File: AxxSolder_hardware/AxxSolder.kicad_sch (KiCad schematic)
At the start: 148 parts, among them IC1 TLV76733DRVR, IC2 OPA2387DSGT, IC3 LMR54406DBVR, IC4 STM32G431CBT6, IC5 TPD4E1U06DBVR, IC6 STUSB4500QTR, IC7 MAX16171ATA_VY+T, IC8 LTC4440AHMS8E, IC9 INA281A5QDBVRQ1, J1 USB4110-GF-A, J2 691243110009, J3 TSW-102-07-T-S, J4 61300611821, J5 TSW-102-07-T-S, J6 TSW-102-07-T-S, Q1 STL9P3LLH6, Q2 STL10N3LLH5, Q3 2N7002NXAKR, U2 PEC11J-9215F-S0015, U3 BSC014N04LS

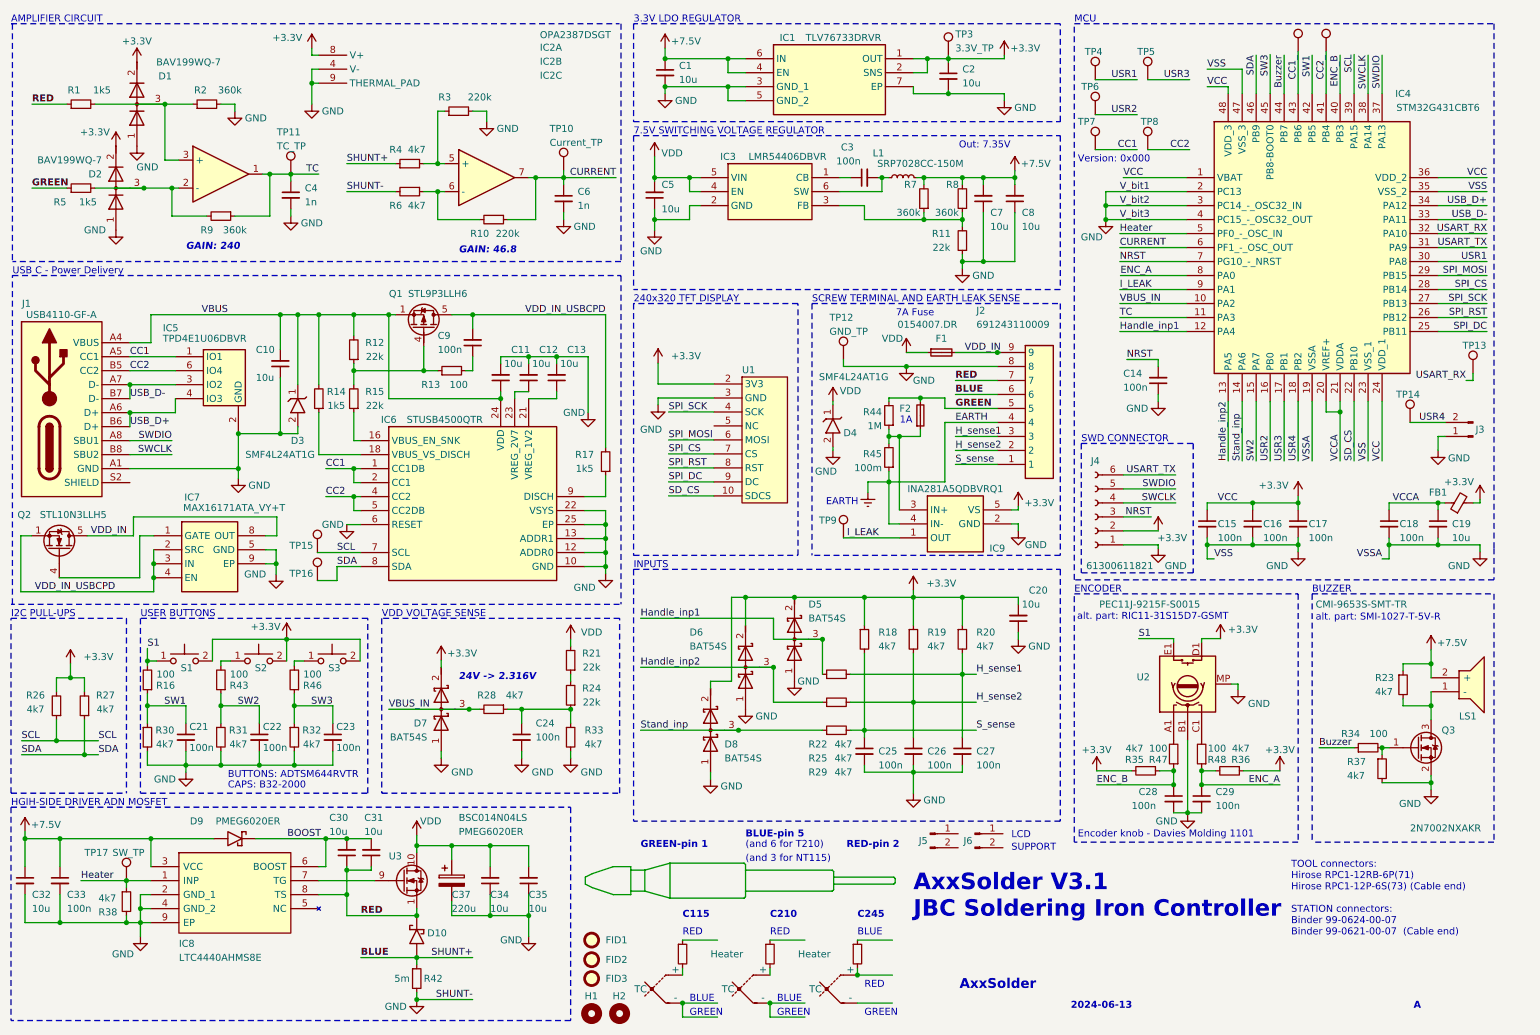
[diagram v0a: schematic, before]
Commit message: Updates on schematic and board layout to hw3_1, optimizations and improvement on layout
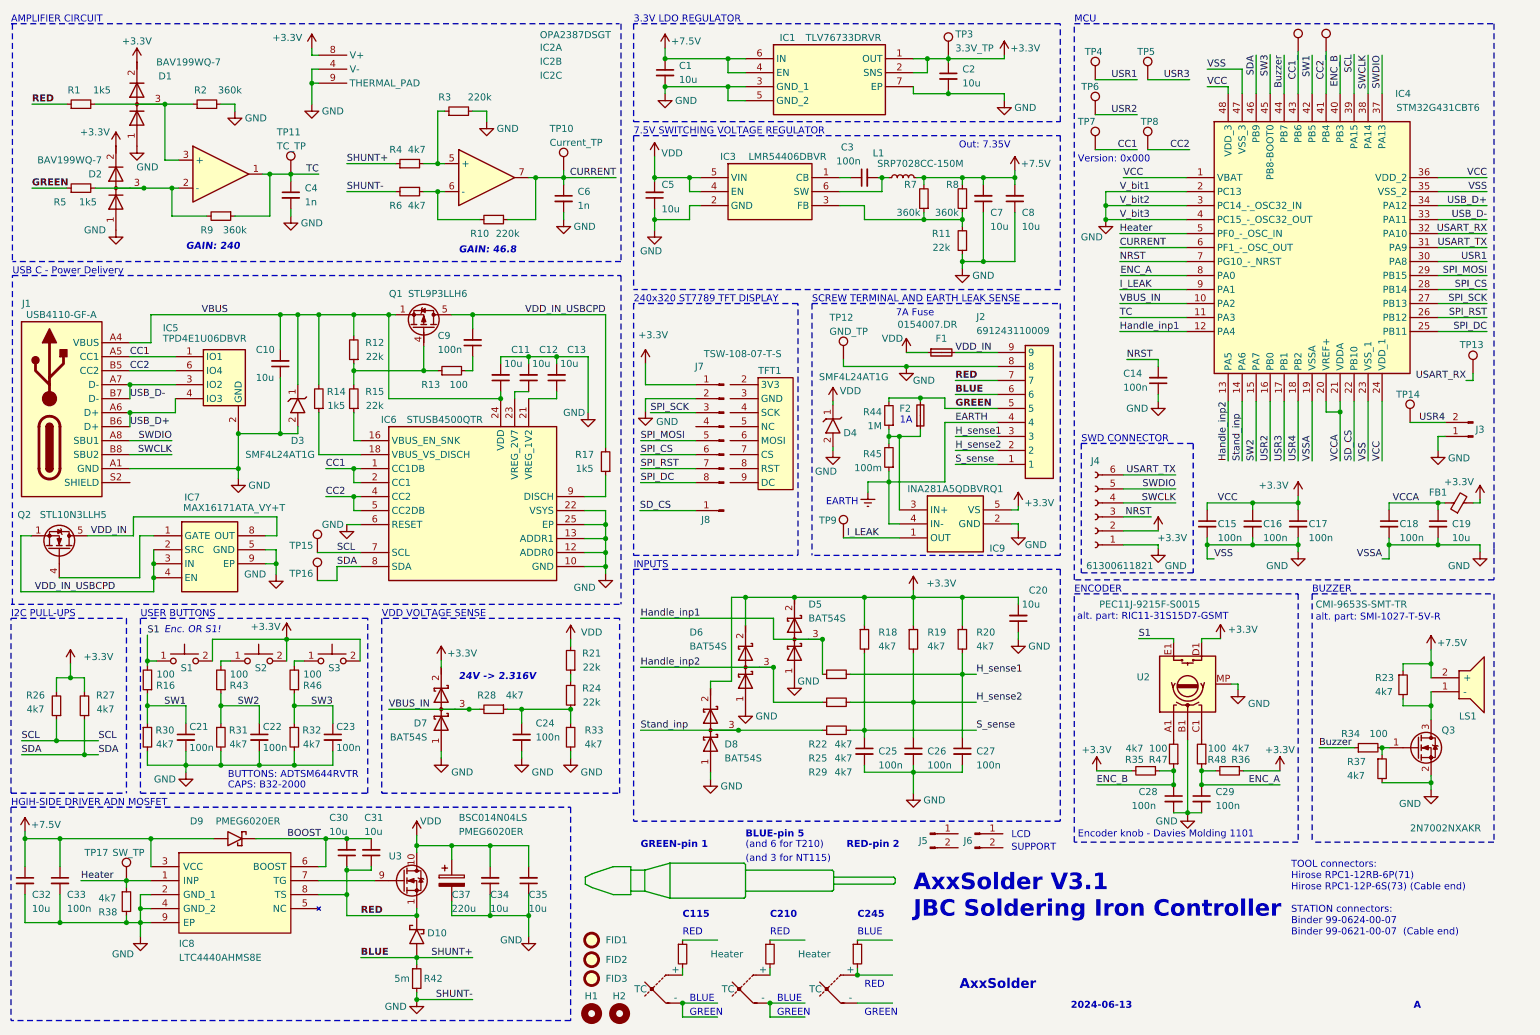
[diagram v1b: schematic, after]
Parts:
- added J7: TSW-108-07-T-S, TSW-108-XX-YY-S, symbol TSW-108-07-T-S:TSW-108-07-T-S
- added J8: Conn_01x01_Pin, symbol Connector:Conn_01x01_Pin
- D5, D6, D7, D8: Manufacturer_Name Diotec Semiconductor -> Nexperia; Manufacturer_Part_Number BAT54S -> BAT54S,215; Mouser Part Number 637-BAT54S -> 771-BAT54S-T/R; Mouser Price/Stock https://www.mouser.co.uk/ProductDetail/Diotec-Semiconductor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 -> https://www.mouser.co.uk/ProductDetail/Nexperia/BAT54S215?q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
- S1: now left out of the parts list
- TP13: footprint Connector_PinSocket_2.54mm:PinSocket_1x01_P2.54mm_Vertical -> footprints:TSW-101-XX-YY-S
- renumbered U1 to TFT1
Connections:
- net +3.3V: now also J7.1 (Pin_1); no longer TFT1.2 (3V3)
- net GND: now also J7.2 (Pin_2); no longer TFT1.3 (GND)
- net SD_CS: now also J8.1 (Pin_1); no longer TFT1.10 (SDCS)
- net SPI_CS: now also J7.6 (Pin_6); no longer TFT1.7 (CS)
- net SPI_DC: now also J7.8 (Pin_8); no longer TFT1.9 (DC)
- net SPI_MOSI: now also J7.5 (Pin_5); no longer TFT1.6 (MOSI)
- net SPI_RST: now also J7.7 (Pin_7); no longer TFT1.8 (RST)
- net SPI_SCK: now also J7.3 (Pin_3); no longer TFT1.4 (SCK)
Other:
- note added: "240x320 ST7789 TFT DISPLAY"
- note added: "Enc. OR S1!"
- note removed: "240x320 TFT DISPLAY"

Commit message: Update footprint name of STL9P3LLH6 to be correct
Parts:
- Q1: footprint footprints:STL20N6F7 -> footprints:STL9P3LLH6
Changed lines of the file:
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@@
       (effects (font (size 1.27 1.27)))
     )
-    (property "Footprint" "footprints:STL20N6F7" (at 69.85 162.992 0)
+    (property "Footprint" "footprints:STL9P3LLH6" (at 69.85 162.992 0)
       (effects (font (size 1.27 1.27)) (justify left top) hide)
     )

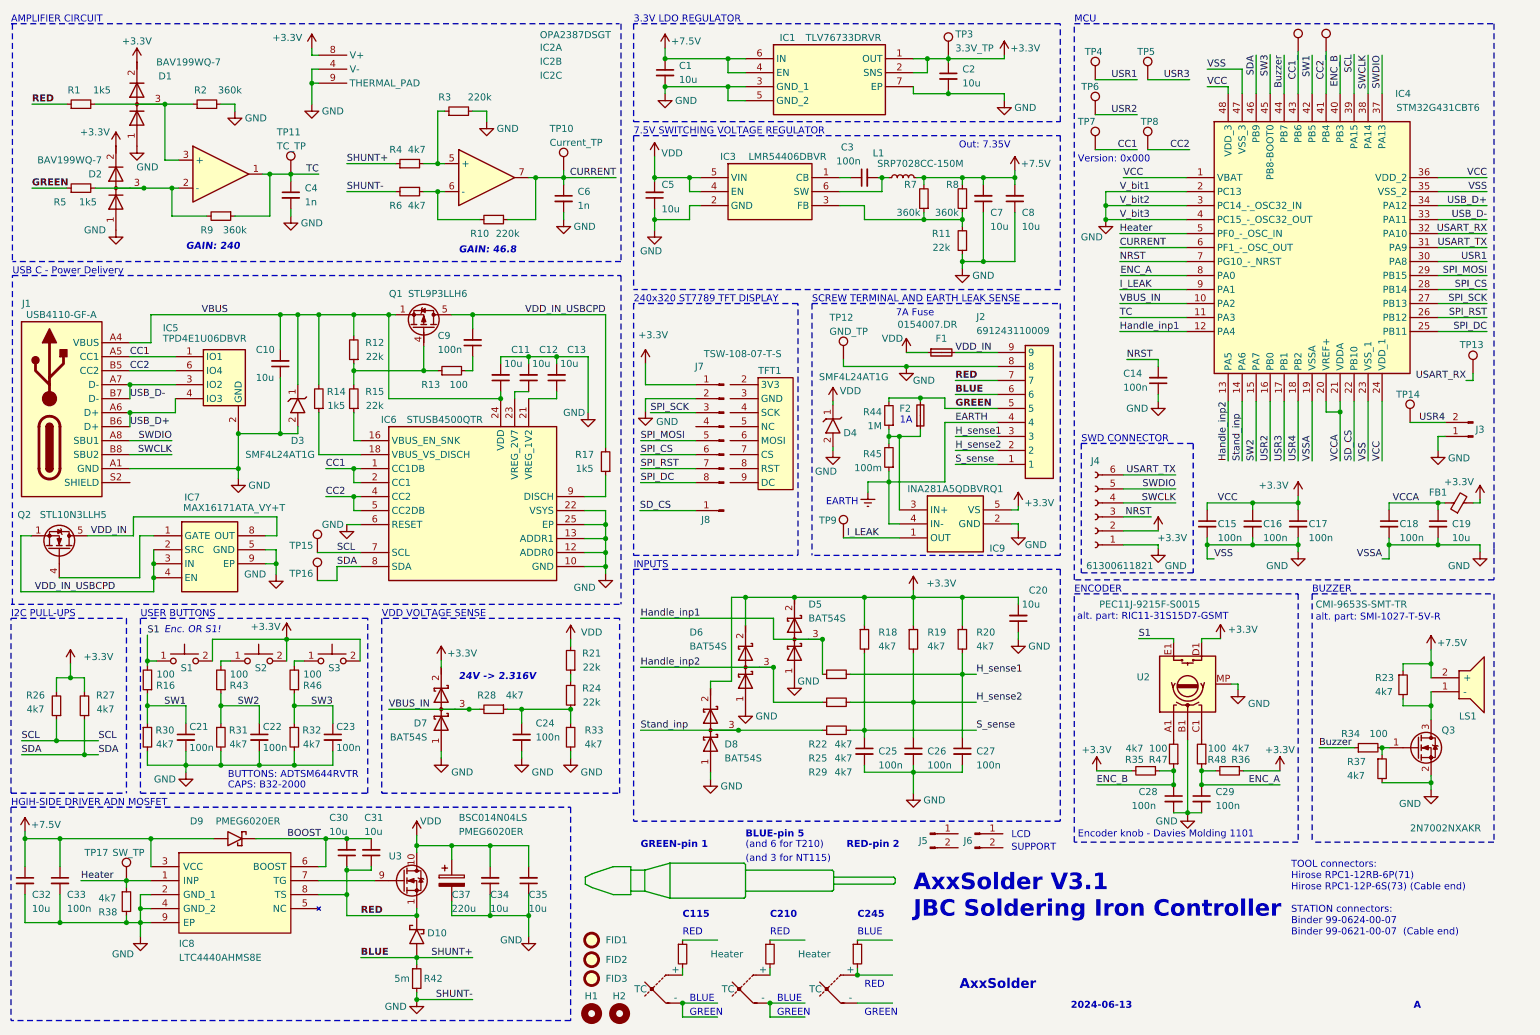
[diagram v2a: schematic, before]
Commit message: Update hardware to 3.2 with changes in layout and addition of series resistors on op-amp outputs
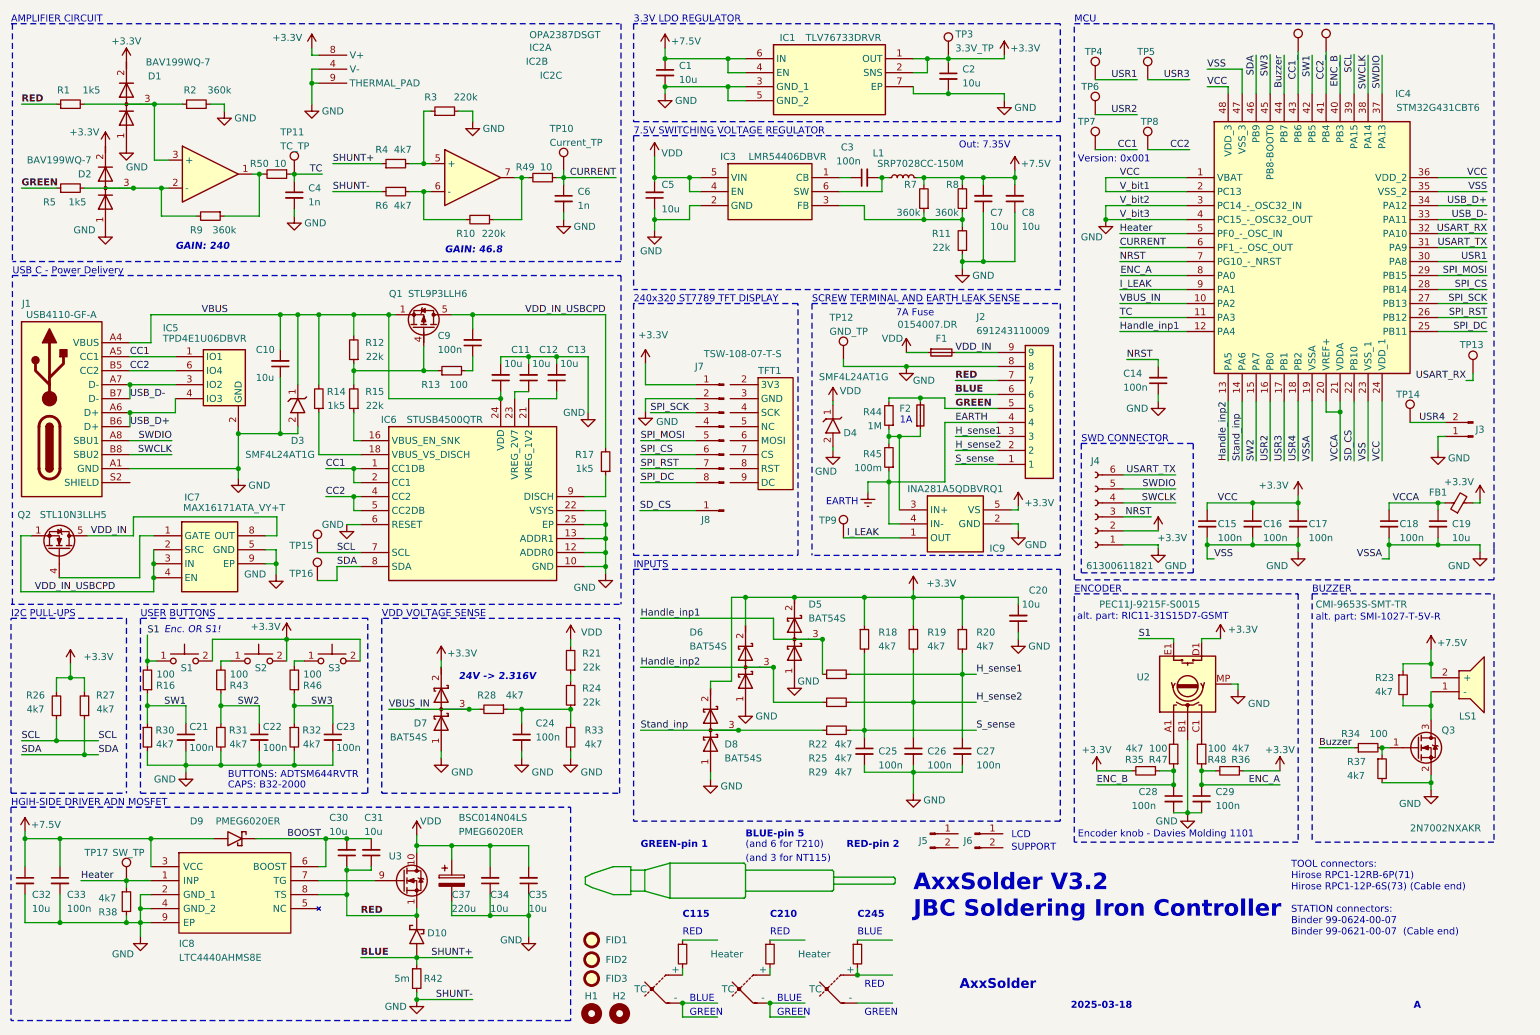
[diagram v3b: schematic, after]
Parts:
- added R49, R50: 10, Resistor_SMD:R_0603_1608Metric, symbol Device:R_Small
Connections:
- net +3.3V: now also IC4.2 (PC13)
- net CURRENT: now also R49.1; no longer IC2.7, R10.1
- net GND: no longer IC4.2 (PC13)
- net TC: now also R50.1; no longer IC2.1, R9.1
- new net: IC2.1, R50.2, R9.1
- new net: IC2.7, R10.1, R49.2
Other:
- note added: "2025-03-18"
- note added: "AxxSolder V3.2 JBC Soldering Iron Controller"
- note added: "Version: 0x001"
- note removed: "2024-06-13"
- note removed: "AxxSolder V3.1 JBC Soldering Iron Controller"
- note removed: "Version: 0x000"
- moved on the sheet: C4, D1, D2, IC2A, IC2B, R1, R10, R2, R3, R4, R5, R6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
